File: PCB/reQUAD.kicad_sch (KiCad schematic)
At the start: 8 parts, among them J1 Model_100_System_BUS, U1 628128, U2 74AC573, U3 74LVC2G79, U4 74AC02

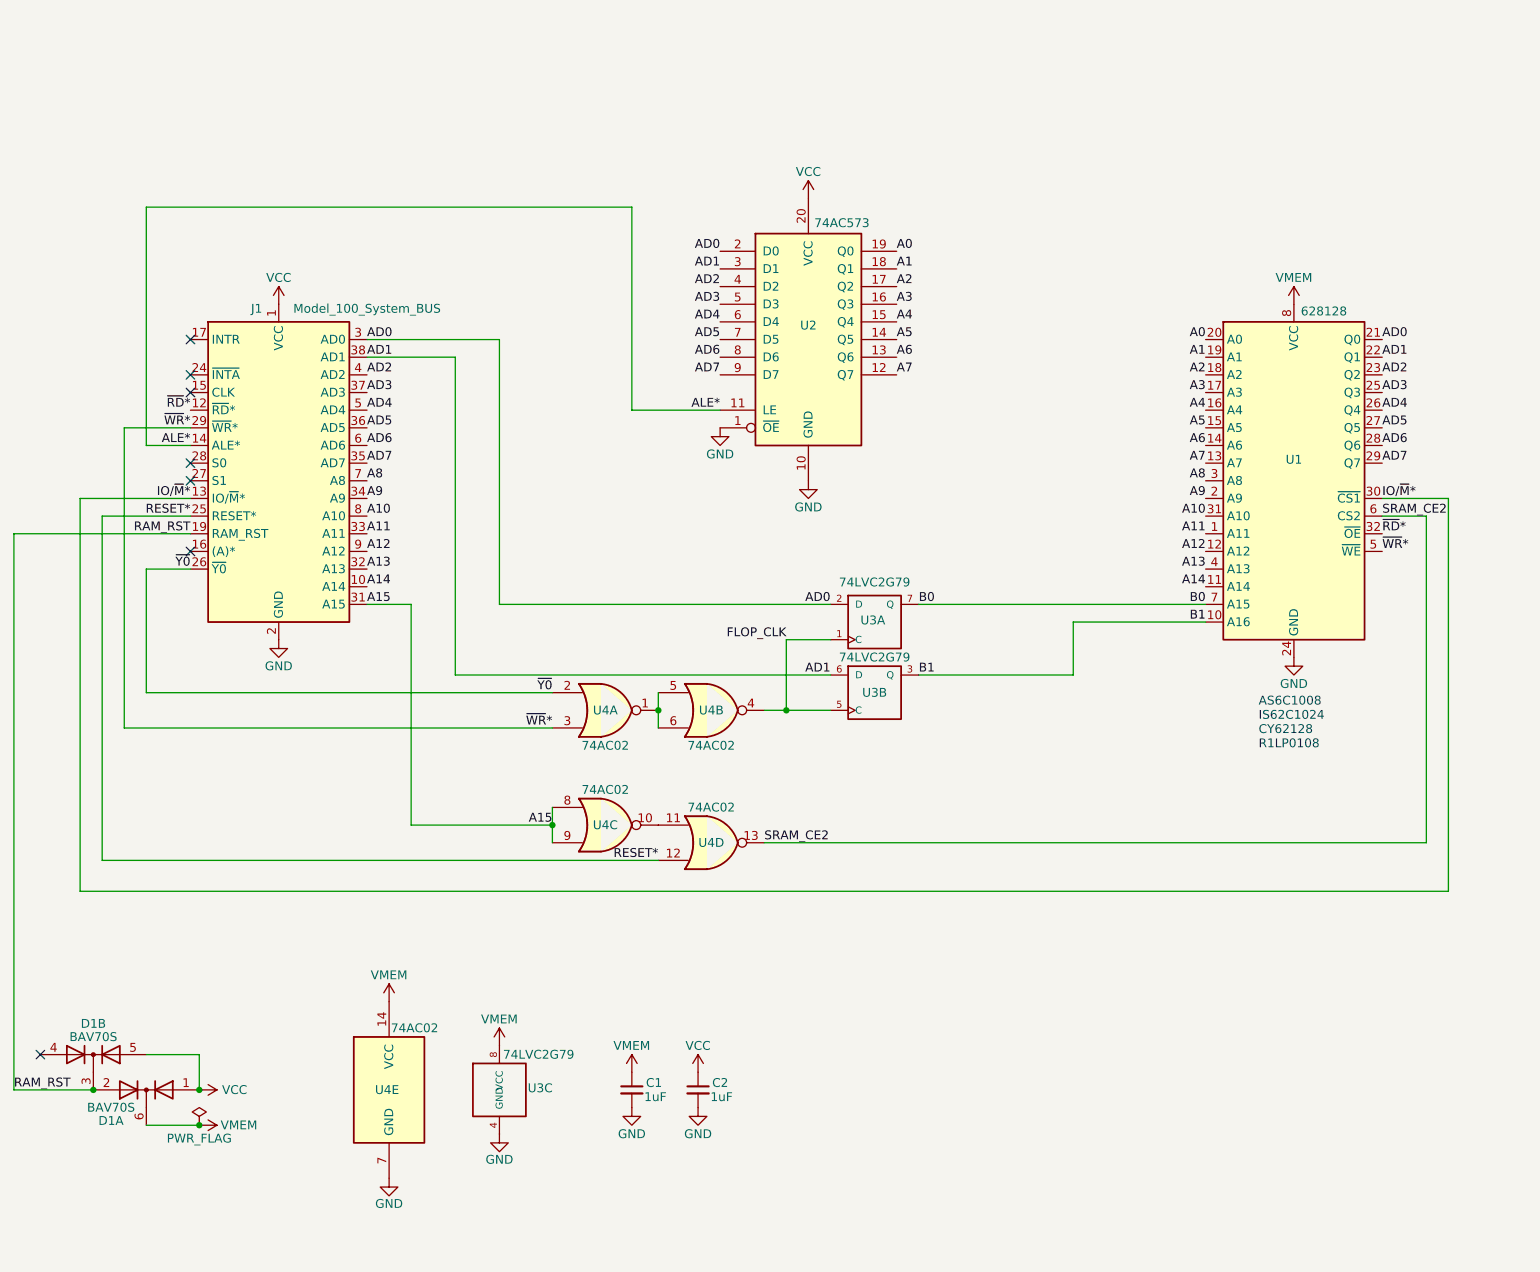
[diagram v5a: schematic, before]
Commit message: standard pins, add 47u on vmem
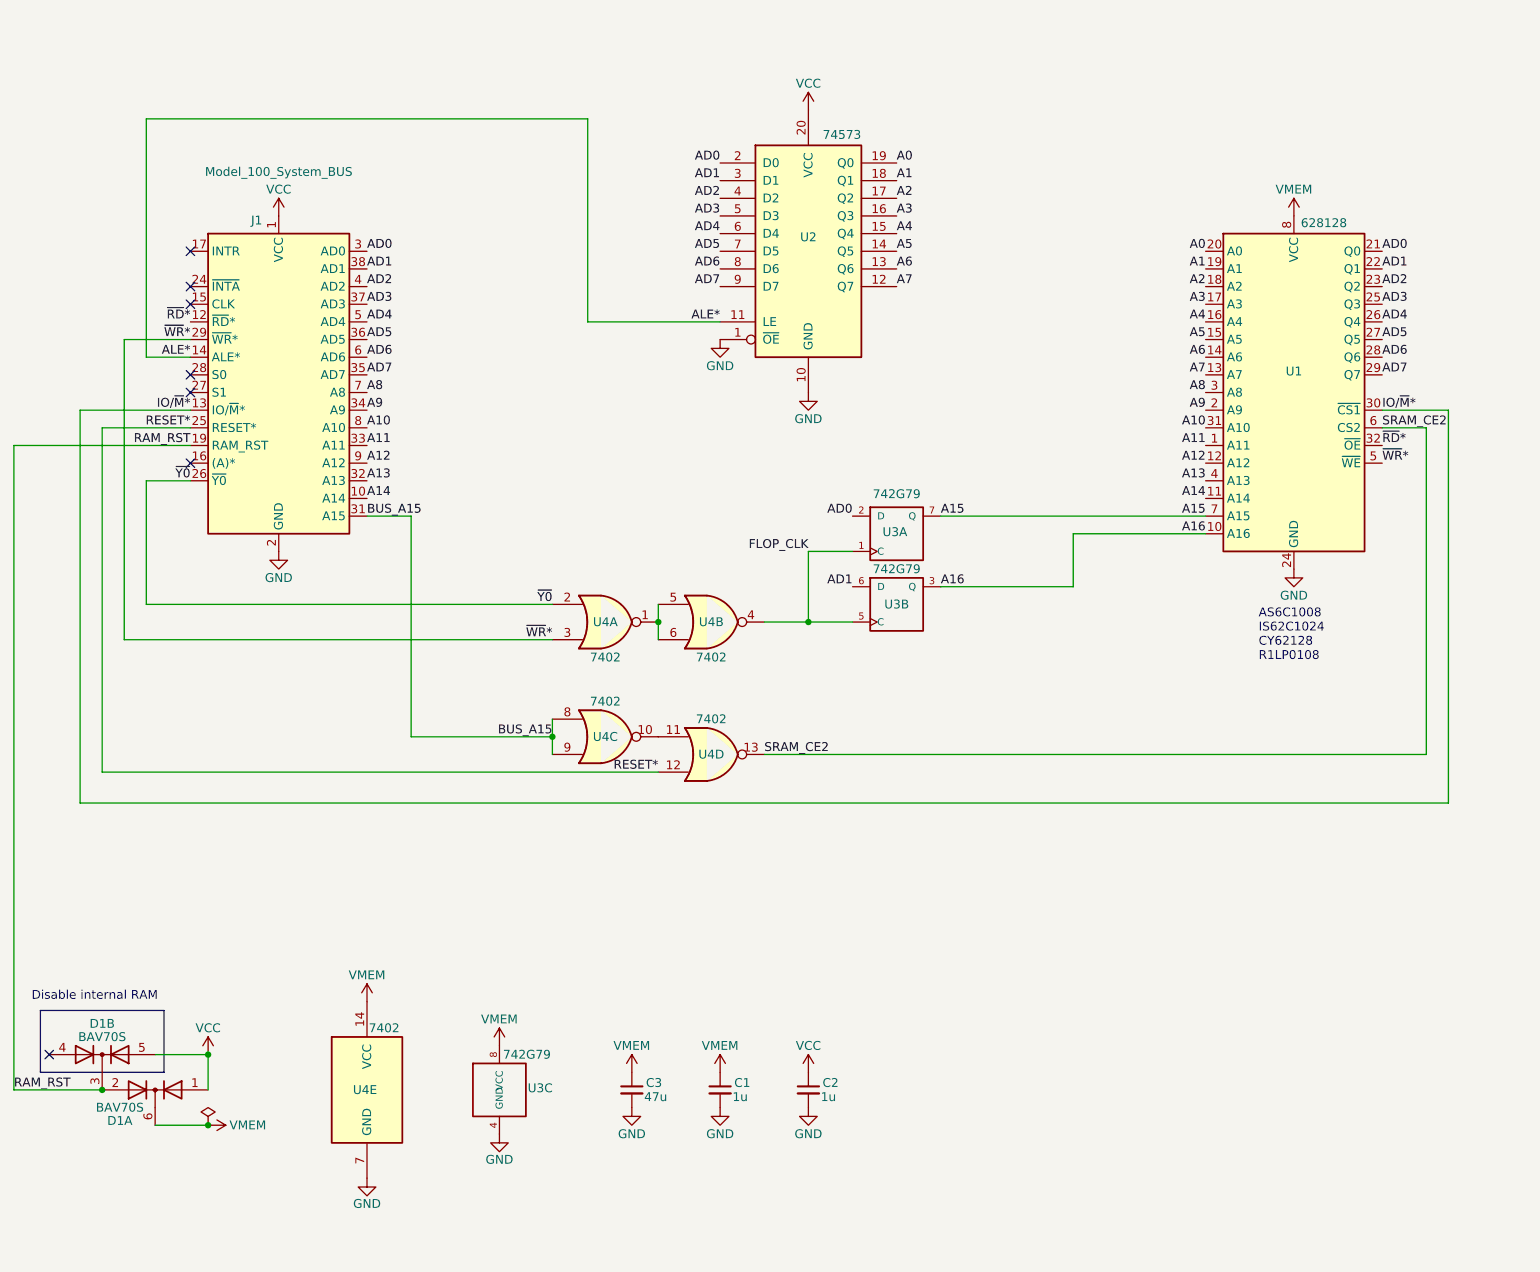
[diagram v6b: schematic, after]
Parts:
- added C3: 47u, 000_LOCAL:C_0805, symbol 000_LOCAL:C_Small
- C1, C2: value 1uF -> 1u
- U2: value 74AC573 -> 74573
- U3: value 74LVC2G79 -> 742G79
- U4: value 74AC02 -> 7402
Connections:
- net B0 is gone; now on net A15: U1.7 (A15), U3.7 (Q)
- net A15: no longer J1.31 (A15), U4.8, U4.9
- net GND: now also C3.2
- net VMEM: now also C3.1
- net B1 renamed A16
- new net BUS_A15: J1.31 (A15), U4.8, U4.9
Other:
- note added: "Disable internal RAM"
- moved on the sheet: C1, C2, D1A, D1B, J1, U1, U2, U3A, U3B, U4A, U4B, U4C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

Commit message: volotile latches, battery
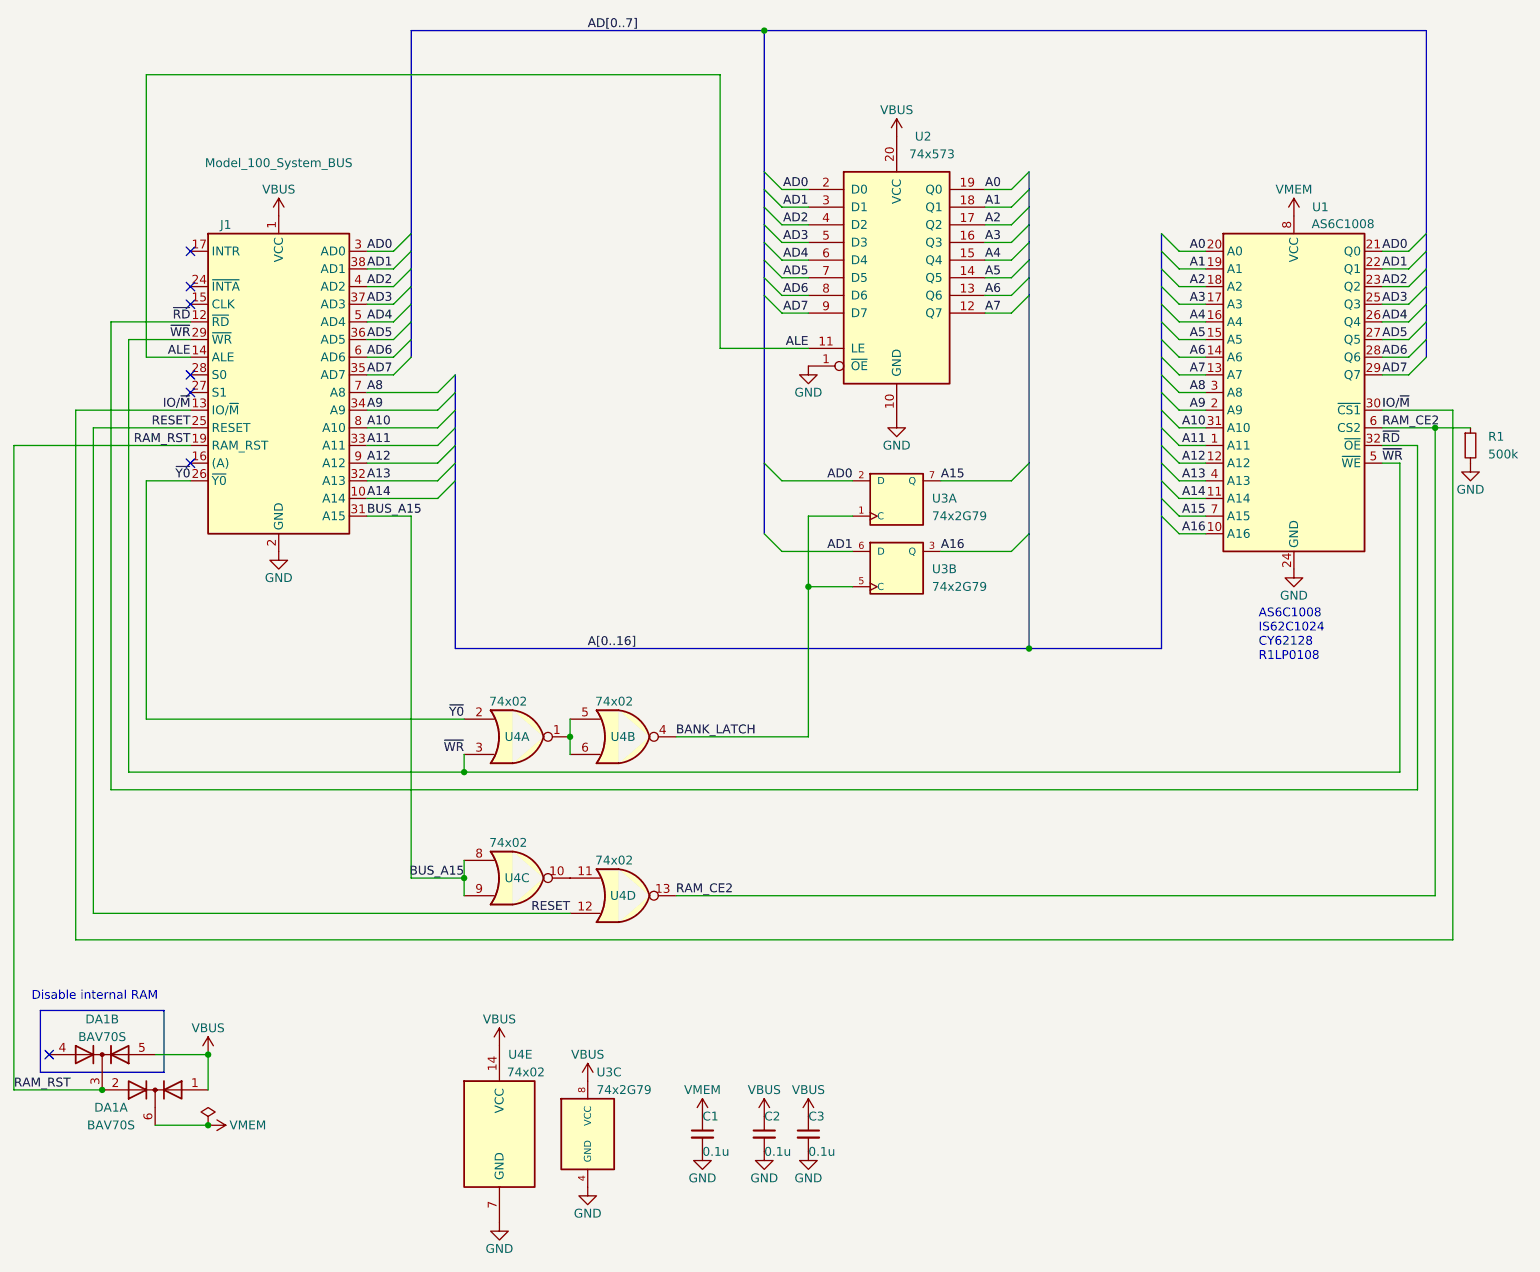
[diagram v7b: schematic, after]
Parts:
- removed D1: BAV70S, 000_LOCAL:SOT-363_symmetric, symbol 000_LOCAL:BAV70S
- added DA1: BAV70S, 000_LOCAL:SOT-363_symmetric, symbol 000_LOCAL:BAV70S
- added R1: 500k, 000_LOCAL:R_0805, symbol 000_LOCAL:R
- C1, C2: value 1u -> 0.1u
- C3: value 47u -> 0.1u
- U1: value 628128 -> AS6C1008
- U2: value 74573 -> 74x573; symbol 000_LOCAL:74573 -> 000_LOCAL:74x573
- U3: value 742G79 -> 74x2G79; symbol 000_LOCAL:74LVC2G79 -> 000_LOCAL:74x2G79
- U4: value 7402 -> 74x02; symbol 000_LOCAL:7402 -> 000_LOCAL:74x02
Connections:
- net GND: now also R1.2
- net RAM_RST: now also DA1.2 (A), DA1.3 (K)
- net VMEM: now also DA1.6 (K); no longer C3.1, U3.8 (VCC), U4.14 (VCC)
- net ALE* renamed ALE
- net FLOP_CLK renamed BANK_LATCH
- net IO/~{M}* renamed IO/~{M}
- net RESET* renamed RESET
- net SRAM_CE2 renamed RAM_CE2
- net RAM_CE2: now also R1.1
- net VCC renamed VBUS
- net VBUS: now also C3.1, U3.8 (VCC), U4.14 (VCC), DA1.1 (A), DA1.5 (A)
- net ~{RD}* renamed ~{RD}
- net ~{WR}* renamed ~{WR}
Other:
- moved on the sheet: C1, C2, U2, U4A, U4B, U4C, U4D, U4E

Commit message: datasheets
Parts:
- C1, C2, C3: value 0.1u -> 1u
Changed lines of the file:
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@@
       (effects (font (size 1.27 1.27)) (justify left))
     )
-    (property "Value" "0.1u" (at 130.81 186.69 0)
+    (property "Value" "1u" (at 130.81 186.69 0)
       (effects (font (size 1.27 1.27)) (justify left))
     )
@@
       (effects (font (size 1.27 1.27)) (justify left))
     )
-    (property "Value" "0.1u" (at 139.7 186.69 0)
+    (property "Value" "1u" (at 139.7 186.69 0)
       (effects (font (size 1.27 1.27)) (justify left))
     )
@@
       (effects (font (size 1.27 1.27)) (justify left))
     )
-    (property "Value" "0.1u" (at 146.05 186.69 0)
-      (effects (font (size 1.27 1.27)) (justify left))
-    )
+    (property "Value" "1u" (at 146.05 186.69 0)
+      (effects (font (size 1.27 1.27)) (justify left))
+    )
